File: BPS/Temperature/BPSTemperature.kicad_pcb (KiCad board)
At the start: 2 copper layers, 82 x 65 mm, 83 parts, among them J1 Conn_02x10_Counter_Clockwise, J2 Logic Analyzer, J3 Conn_02x06_Counter_Clockwise, J4 Conn_02x06_Counter_Clockwise, J5 Conn_01x02, SW1 SW_DIP_x06, U1 LTC2983

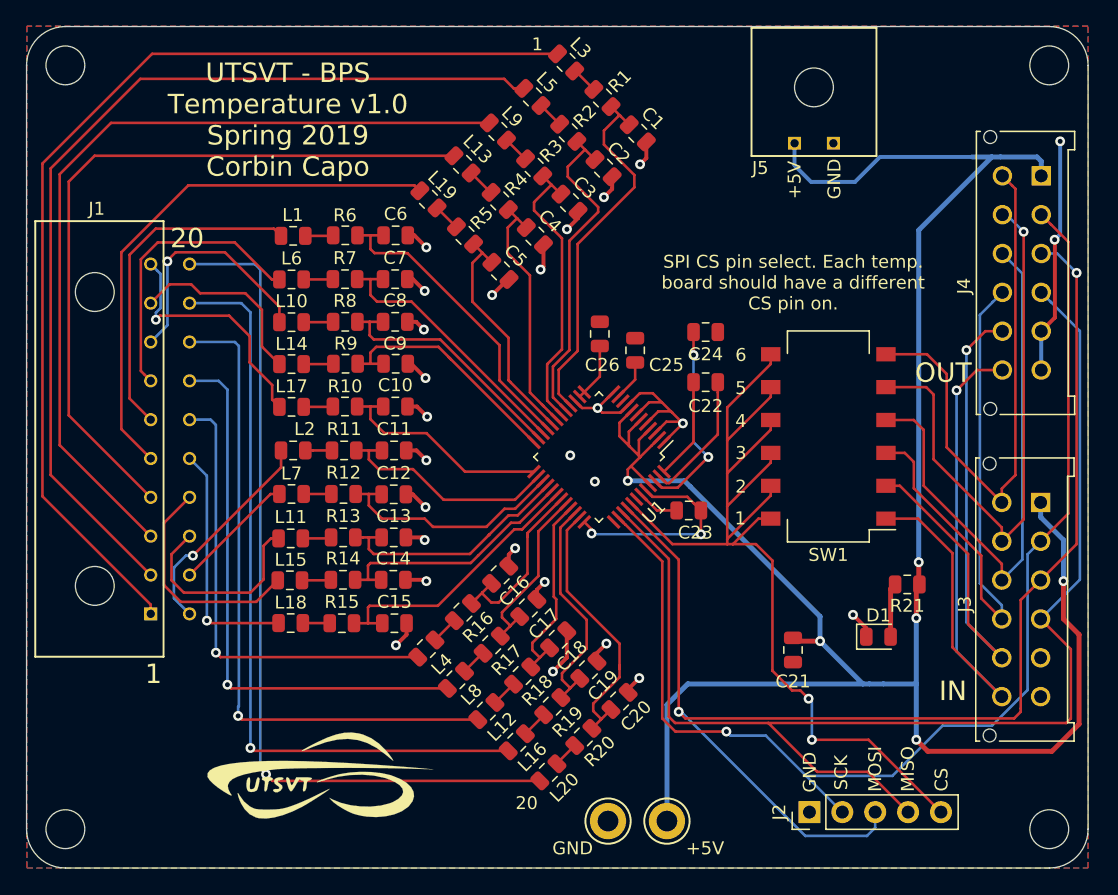
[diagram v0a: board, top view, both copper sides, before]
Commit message: Edited BPS temperature board to have stackable connectors.
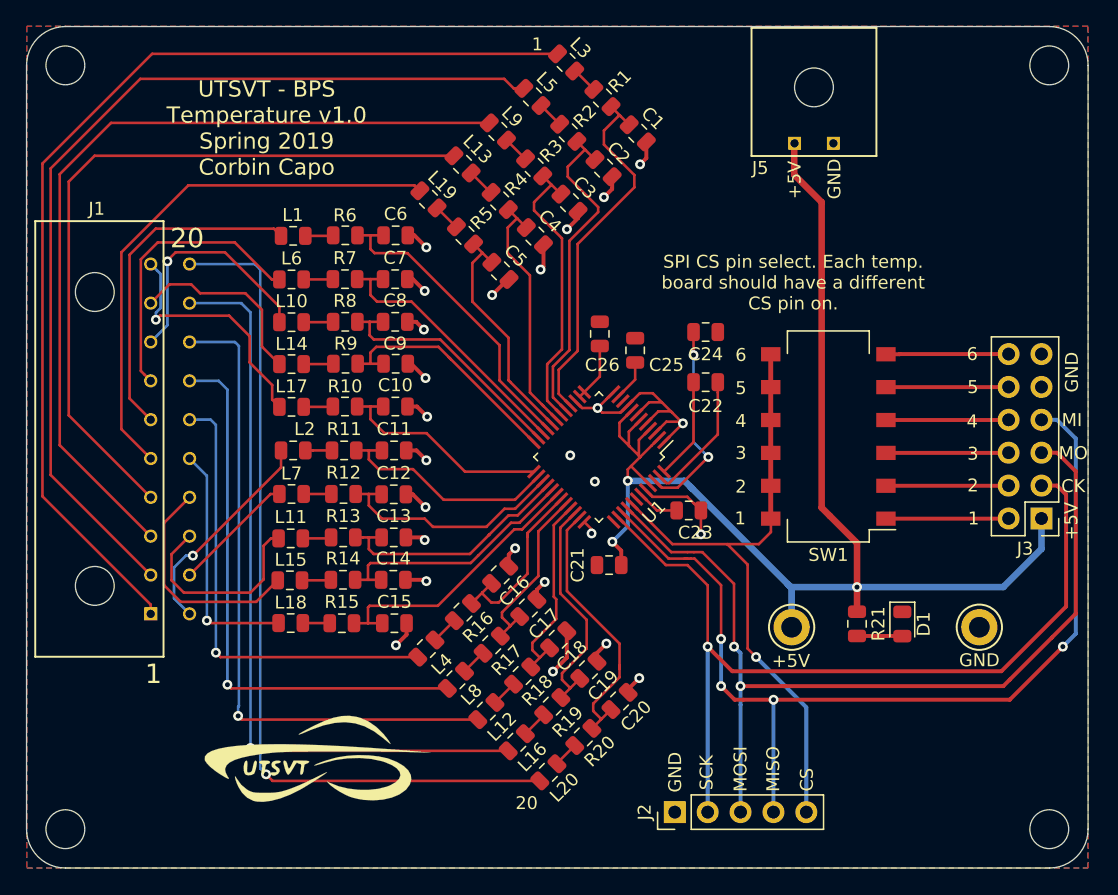
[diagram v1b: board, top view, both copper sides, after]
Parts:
- removed +5V, GND: TestPoint, TestPoint:TestPoint_Keystone_5005-5009_Compact
- removed J4: Conn_02x06_Counter_Clockwise, UTSVT_Connectors:Molex_MicroFit3.0_2x6xP3.00mm_PolarizingPeg_Vertical
- added TP1: TestPoint, TestPoint:TestPoint_Keystone_5005-5009_Compact, F.Cu at (112.1, 116.4)
- added TP2: TestPoint, TestPoint:TestPoint_Keystone_5005-5009_Compact, F.Cu at (126.6, 116.4)
- J3: footprint UTSVT_Connectors:Molex_MicroFit3.0_2x6xP3.00mm_PolarizingPeg_Vertical -> Connector_PinHeader_2.54mm:PinHeader_2x06_P2.54mm_Vertical
- moved C21 15.6 mm to (98.0, 111.6), turned to 0 degrees
- moved J2 10.4 mm to (103.1, 130.7)
- moved R21 4.93 mm to (117.2, 116.1), turned to 270 degrees
- moved D1 2.09 mm to (120.7, 116.2), turned to 270 degrees
- moved G*** 1.31 mm to (75.2, 126.7)
- moved J3 1.24 mm to (131.4, 108.0), turned to 180 degrees
- moved G*** 1.04 mm to (84.2, 100.9)
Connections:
- J3 pad 10: /CS3 -> /CS5
- J3 pad 11: /CS2 -> GND
- J3 pad 12: /CS1 -> /CS6
- J3 pad 2: /SCK -> /CS1
- J3 pad 3: /MOSI -> /SCK
- J3 pad 4: /MISO -> /CS2
- J3 pad 5: GND -> /MOSI
- J3 pad 6: GND -> /CS3
- J3 pad 7: /CS6 -> /MISO
- J3 pad 8: /CS5 -> /CS4
- J3 pad 9: /CS4 -> GND
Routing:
- net +5V: track 176.2 -> 104.5 mm, vias 6 -> 3
- net /CS1: track 48.2 -> 9.45 mm, vias 1 -> 0
- net /CS2: track 45.9 -> 9.49 mm, vias 1 -> 0
- net /CS5: track 44.2 -> 9.52 mm, vias 1 -> 0
- net /CS3: track 44.0 -> 9.48 mm
- net /CS4: track 43.9 -> 9.47 mm
- net /CS6: track 43.1 -> 9.52 mm
- net /MOSI: track 103.9 -> 71.1 mm
- net /CS1_OUT: track 82.3 -> 49.5 mm, vias 2 -> 1
- net GND: track 95.6 -> 66.8 mm, vias 29 -> 26
- net /SCK: track 92.6 -> 68.0 mm
- net /MISO: track 98.6 -> 74.9 mm, vias 0 -> 4
- net Net-(D1-Pad2): track 4.19 -> 3.62 mm
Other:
- board text added: "CK"
- board text added: "MI"
- board text added: "MO"
- board text removed: "IN"
- board text removed: "OUT"

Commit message: Updated connectors **Use new netlist**
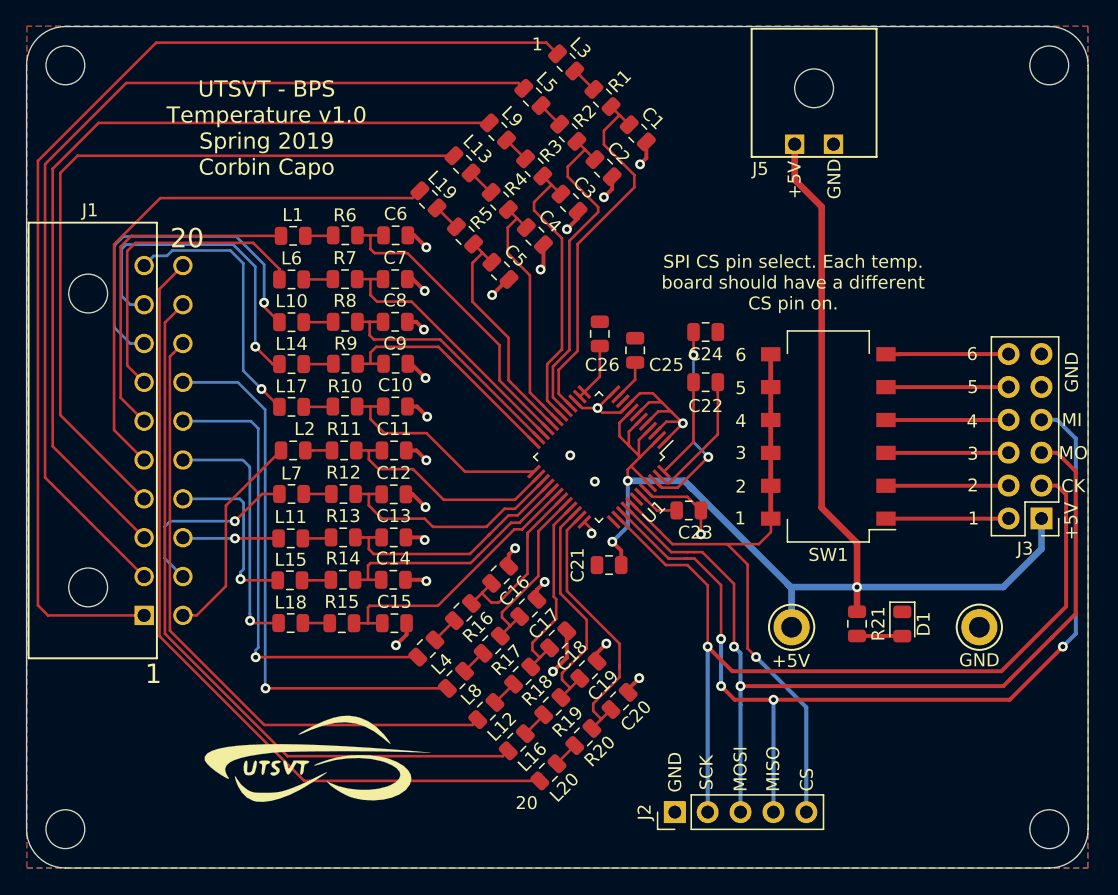
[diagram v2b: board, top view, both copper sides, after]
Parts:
- moved J1 0.53 mm to (65.4, 118.8)
- moved J5 0.07 mm to (109.0, 80.1)
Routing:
- net /CH9_LPF: track 14.8 -> 25.4 mm, vias 0 -> 1
- net /CH13_LPF: track 15.9 -> 7.41 mm, vias 0 -> 1
- net /CH8_LPF: track 18.7 -> 26.8 mm
- net /CH1_LPF: track 81.5 -> 87.1 mm
- net /CH12_LPF: track 9.53 -> 14.3 mm, vias 0 -> 1
- net /CH14_LPF: track 17.6 -> 13.7 mm, vias 0 -> 1
- net /CH7_LPF: track 22.1 -> 25.1 mm
- net /CH20_LPF: track 66.2 -> 63.4 mm, vias 1 -> 0
- net /CH19_LPF: track 58.7 -> 56.6 mm, vias 1 -> 0
- net /CH18_LPF: track 51.2 -> 49.6 mm, vias 1 -> 0
- net /CH10_LPF: track 19.2 -> 20.8 mm
- net /CH4_LPF: track 57.6 -> 58.8 mm
- net /CH3_LPF: track 65.7 -> 66.6 mm
- net /CH15_LPF: track 18.7 -> 19.6 mm
- net /CH16_LPF: track 35.5 -> 36.3 mm
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
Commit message: fixed bugs
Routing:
- net /CH13_LPF: track 7.41 -> 30.7 mm, vias 1 -> 2
- net /CH10_LPF: track 20.8 -> 16.9 mm
- net /CH18_LPF: track 49.6 -> 47.3 mm, vias 0 -> 2
- net /CH15_LPF: track 19.6 -> 20.3 mm
- net /CH11_LPF: track 16.5 -> 17.1 mm

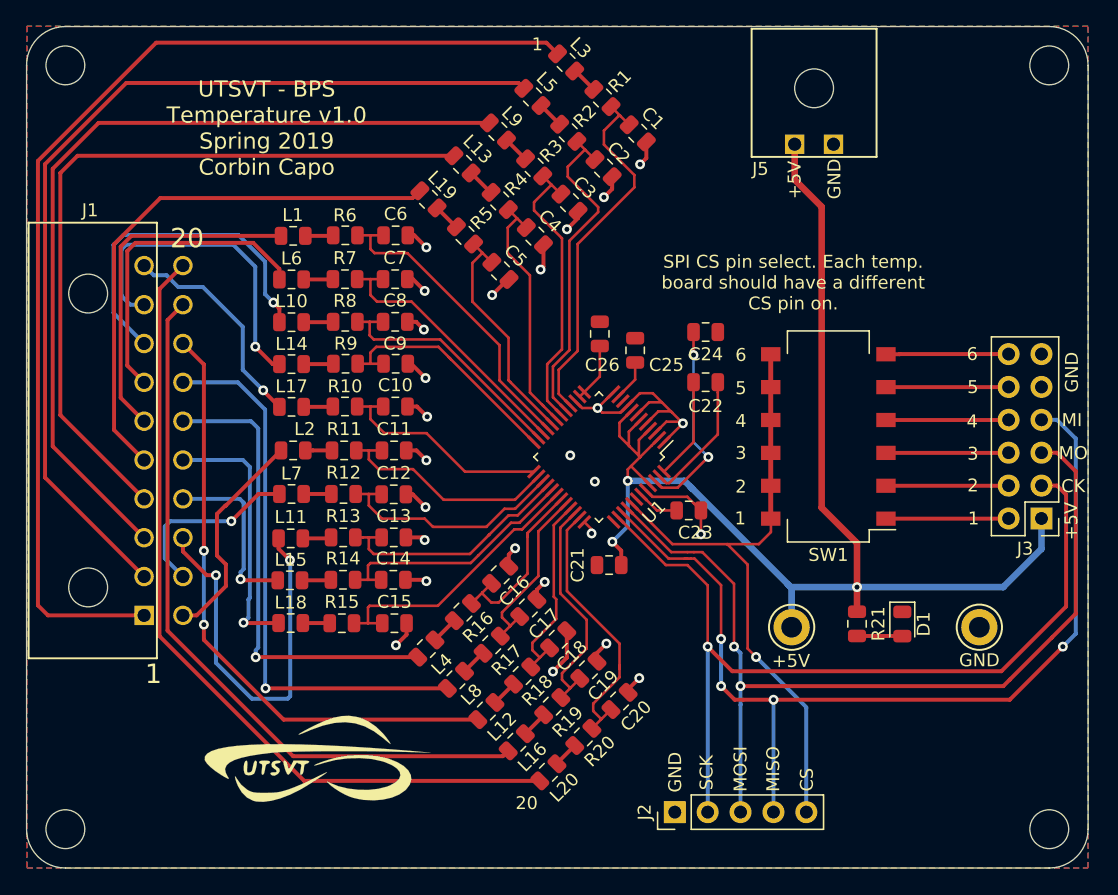
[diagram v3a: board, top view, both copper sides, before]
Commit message: Fixed temperature board for BPS.
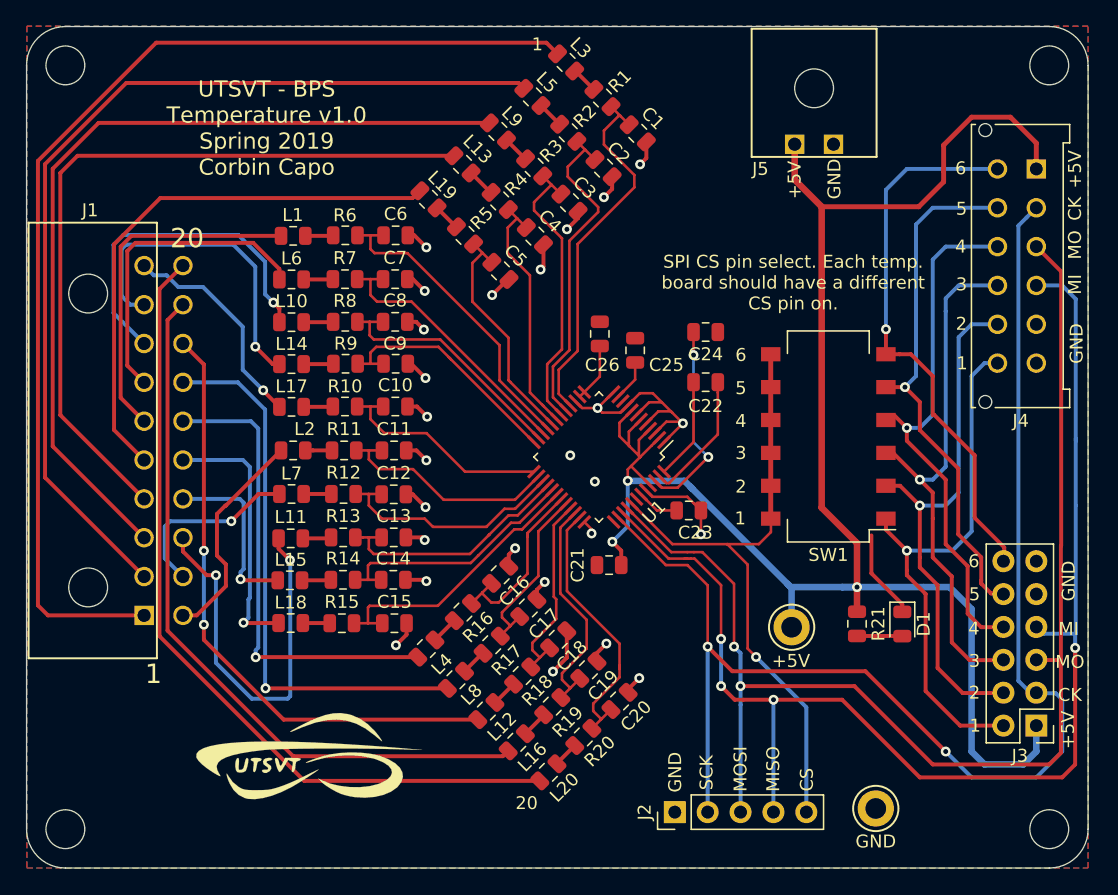
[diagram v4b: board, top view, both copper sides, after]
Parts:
- added J4: Conn_02x06_Counter_Clockwise, UTSVT_Connectors:Molex_MicroFit3.0_2x6xP3.00mm_PolarizingPeg_Vertical, F.Cu at (131.0, 81.0)
- moved TP2 16.1 mm to (118.6, 130.4)
- moved J3 16.0 mm to (131.0, 124.0)
- moved G*** 0.68 mm to (74.5, 126.5)
- moved G*** 0.40 mm to (83.9, 100.6)
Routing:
- net /SCK: track 68.0 -> 104.1 mm, vias 1 -> 2
- net +5V: track 104.4 -> 140.0 mm
- net /CS6: track 9.52 -> 43.2 mm, vias 0 -> 1
- net /CS1: track 9.45 -> 42.0 mm, vias 0 -> 1
- net /CS3: track 9.48 -> 41.6 mm, vias 0 -> 1
- net /CS2: track 9.49 -> 40.9 mm, vias 0 -> 1
- net /CS5: track 9.52 -> 40.9 mm, vias 0 -> 1
- net /CS4: track 9.47 -> 40.7 mm, vias 0 -> 1
- net /MISO: track 74.9 -> 102.9 mm
- net /MOSI: track 71.1 -> 98.3 mm
- net GND: track 66.8 -> 73.7 mm

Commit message: Edited temmperature board to have reset pin to high.
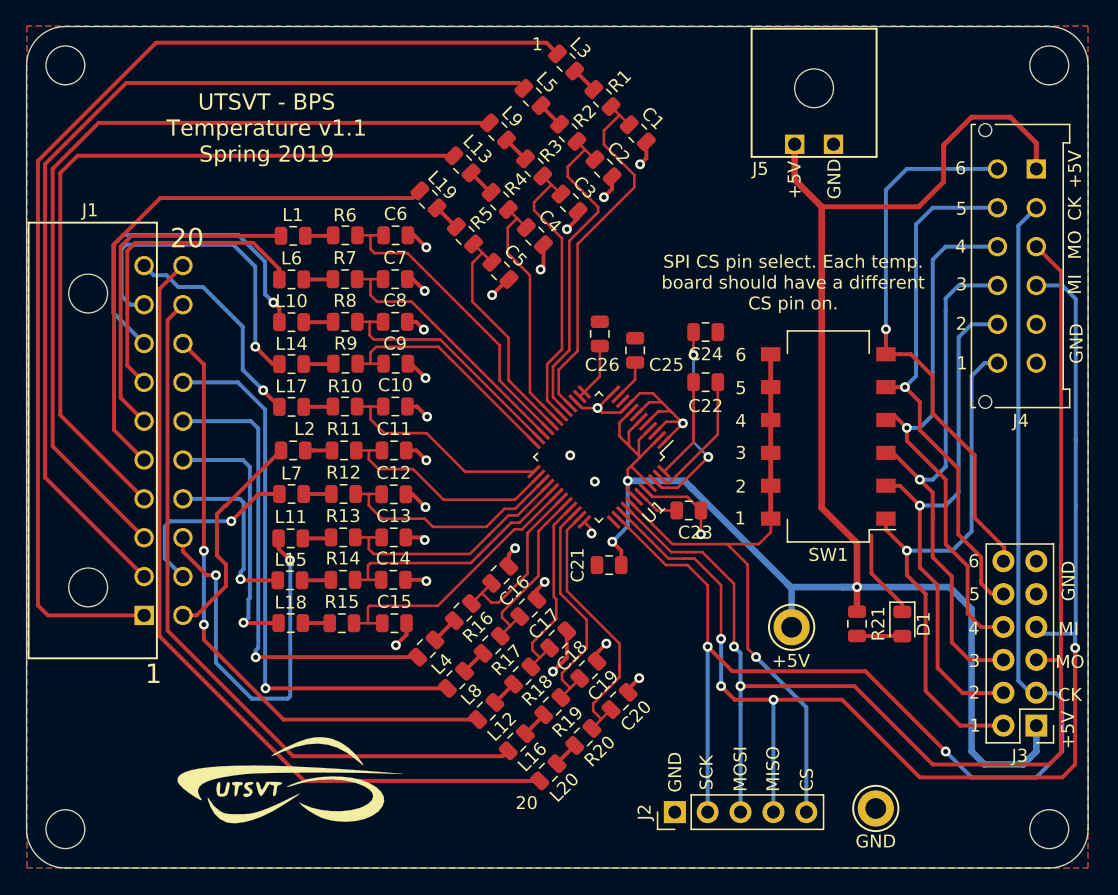
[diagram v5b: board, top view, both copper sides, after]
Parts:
- C1, C10, C11, C12, C13, C14, C15, C16, C17, C18, C19, C2, C20, C3, C4, C5, C6, C7, C8, C9: value 1uF -> 0.1uF
- R1, R10, R11, R12, R13, R14, R15, R16, R17, R18, R19, R2, R20, R3, R4, R5, R6, R7, R8, R9: value 1k -> 1.5k
- moved G*** 2.36 mm to (73.1, 128.3)
- moved G*** 0.28 mm to (83.8, 100.8)
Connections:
- U1 pad 42: Net-(U1-Pad42) -> +5V
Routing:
- net +5V: track 140.0 -> 141.7 mm
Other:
- board text added: "UTSVT - BPS Temperature v1.1 Spring 2019"
- board text removed: "UTSVT - BPS Temperature v1.0 Spring 2019 Corbin Capo"
